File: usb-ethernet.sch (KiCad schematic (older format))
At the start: 17 parts

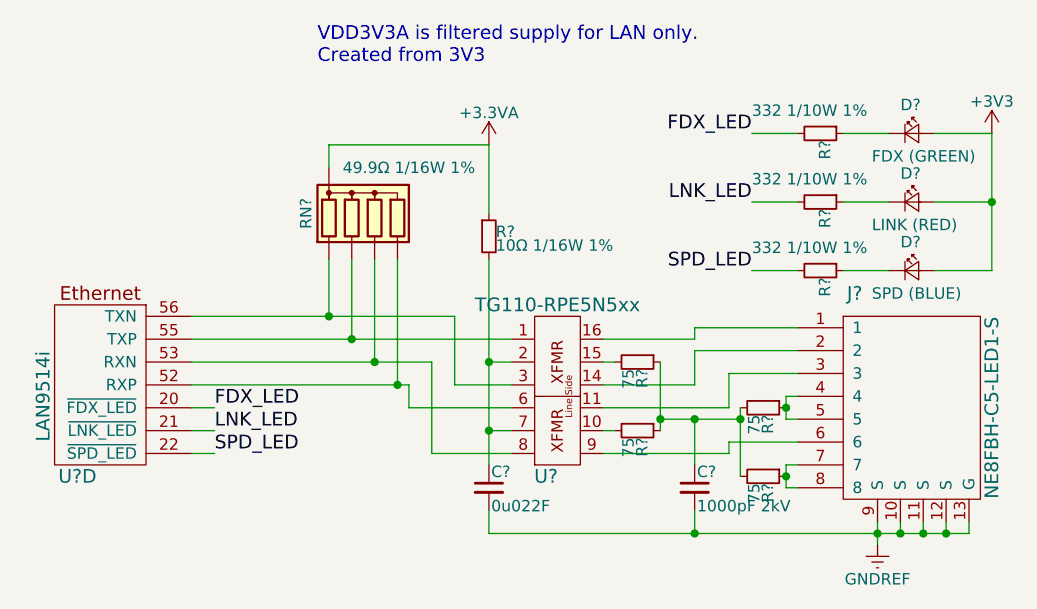
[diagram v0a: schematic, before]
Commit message: Started fixing DRC issues
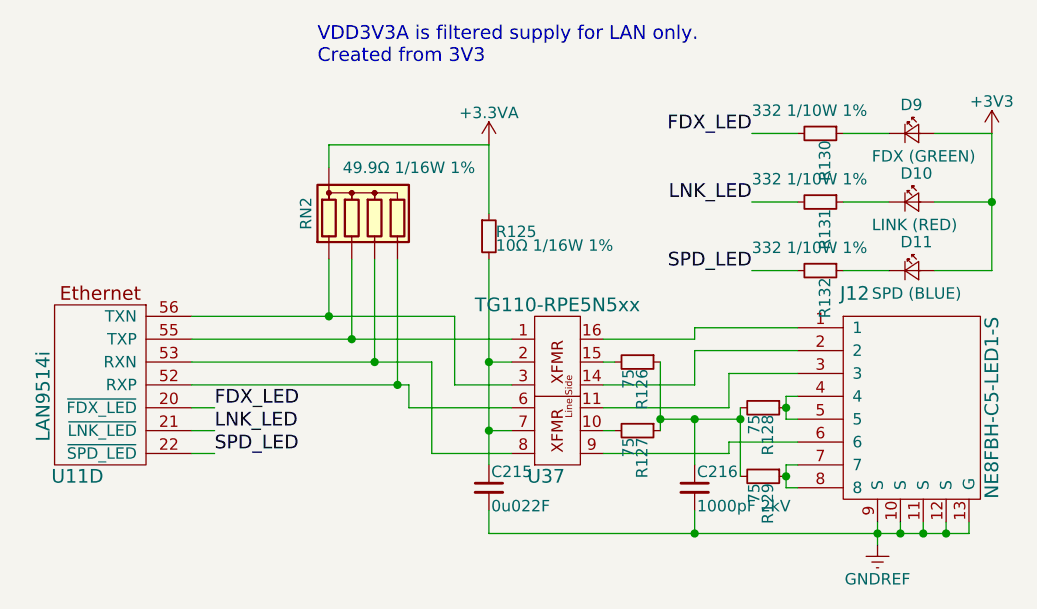
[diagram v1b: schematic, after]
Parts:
- C215, C216: renamed from C?; footprint (none) -> Capacitors_SMD:C_0603_HandSoldering
- R125, R126, R127, R128, R129, R130, R131, R132: renamed from R?; footprint (none) -> Capacitors_SMD:C_0603_HandSoldering
- U11: renamed from U?; footprint (none) -> Housings_DFN_QFN:QFN-64-1EP_9x9mm_Pitch0.5mm
- gave numbers to parts that had none: 6
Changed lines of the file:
@@
 P 3550 3750
 AR Path="/58DEDA35/5903ABC9" Ref="U?"  Part="4"
-AR Path="/58DEDA35/5903AB75/5903ABC9" Ref="U?"  Part="4"
-F 0 "U?" H 3650 3350 60  0000 C CNN
+AR Path="/58DEDA35/5903AB75/5903ABC9" Ref="U11"  Part="4"
+F 0 "U11" H 3650 3350 60  0000 C CNN
 F 1 "LAN9514i" V 3800 3700 60  0000 C CNN
-F 2 "" H 4250 4250 60  0001 C CNN
+F 2 "Housings_DFN_QFN:QFN-64-1EP_9x9mm_Pitch0.5mm" H 4250 4250 60  0001 C CNN
 F 3 "http://ww1.microchip.com/downloads/en/DeviceDoc/00002306A.pdf" H 3700 5400 60  0001 C CNN
 F 4 "Microchip Technology" H 3450 5100 60  0001 C CNN "Manufacturer"
@@
 $EndComp
 $Comp
-L TG110-RPE5N5xx U?
+L TG110-RPE5N5xx U37
 U 1 1 590032EB
 P 5550 3800
-F 0 "U?" H 5500 4150 60  0000 C CNN
+F 0 "U37" H 5500 4150 60  0000 C CNN
 F 1 "TG110-RPE5N5xx" H 5550 3400 60  0000 C CNN
 F 2 "" H 5050 4000 60  0001 C CNN
@@
 $EndComp
 $Comp
-L NE8FBH-C5-LED1-S J?
+L NE8FBH-C5-LED1-S J12
 U 1 1 5900332E
 P 7100 3800
-F 0 "J?" H 6850 4250 60  0000 C CNN
+F 0 "J12" H 6850 4250 60  0000 C CNN
 F 1 "NE8FBH-C5-LED1-S" V 7450 3750 60  0000 C CNN
 F 2 "" H 7000 3700 60  0001 C CNN
@@
 $EndComp
 $Comp
-L R_Small R?
+L R_Small R126
 U 1 1 5900376D
 P 5900 3650
-F 0 "R?" H 5930 3670 50  0000 L CNN
+F 0 "R126" H 5930 3670 50  0000 L CNN
 F 1 "75" H 5930 3610 50  0000 L CNN
-F 2 "" H 5900 3650 50  0001 C CNN
+F 2 "Capacitors_SMD:C_0603_HandSoldering" H 5900 3650 50  0001 C CNN
 F 3 "" H 5900 3650 50  0001 C CNN
 	1    5900 3650
@@
 $EndComp
 $Comp
-L R_Small R?
+L R_Small R127
 U 1 1 590037C5
 P 5900 3950
-F 0 "R?" H 5930 3970 50  0000 L CNN
+F 0 "R127" H 5930 3970 50  0000 L CNN
 F 1 "75" H 5930 3910 50  0000 L CNN
-F 2 "" H 5900 3950 50  0001 C CNN
+F 2 "Capacitors_SMD:C_0603_HandSoldering" H 5900 3950 50  0001 C CNN
 F 3 "" H 5900 3950 50  0001 C CNN
 	1    5900 3950
@@
 $EndComp
 $Comp
-L R_Small R?
+L R_Small R128
 U 1 1 5900382C
 P 6450 3850
-F 0 "R?" H 6480 3870 50  0000 L CNN
+F 0 "R128" H 6480 3870 50  0000 L CNN
 F 1 "75" H 6480 3810 50  0000 L CNN
-F 2 "" H 6450 3850 50  0001 C CNN
+F 2 "Capacitors_SMD:C_0603_HandSoldering" H 6450 3850 50  0001 C CNN
 F 3 "" H 6450 3850 50  0001 C CNN
 	1    6450 3850
@@
 $EndComp
 $Comp
-L R_Small R?
+L R_Small R129
 U 1 1 59003855
 P 6450 4150
-F 0 "R?" H 6480 4170 50  0000 L CNN
+F 0 "R129" H 6480 4170 50  0000 L CNN
 F 1 "75" H 6480 4110 50  0000 L CNN
-F 2 "" H 6450 4150 50  0001 C CNN
+F 2 "Capacitors_SMD:C_0603_HandSoldering" H 6450 4150 50  0001 C CNN
 F 3 "" H 6450 4150 50  0001 C CNN
 	1    6450 4150
@@
 $EndComp
 $Comp
-L C_Small C?
+L C_Small C216
 U 1 1 5900394D
 P 6150 4200
-F 0 "C?" H 6160 4270 50  0000 L CNN
+F 0 "C216" H 6160 4270 50  0000 L CNN
 F 1 "1000pF 2kV" H 6160 4120 50  0000 L CNN
-F 2 "" H 6150 4200 50  0001 C CNN
+F 2 "Capacitors_SMD:C_0603_HandSoldering" H 6150 4200 50  0001 C CNN
 F 3 "" H 6150 4200 50  0001 C CNN
 F 4 "0.00@0" H 6150 4200 60  0001 C CNN "Pricing"
@@
 $EndComp
 $Comp
-L GNDREF #PWR?
+L GNDREF #PWR0163
 U 1 1 59003AB4
 P 6950 4450
-F 0 "#PWR?" H 6950 4200 50  0001 C CNN
+F 0 "#PWR0163" H 6950 4200 50  0001 C CNN
 F 1 "GNDREF" H 6950 4300 50  0000 C CNN
 F 2 "" H 6950 4450 50  0001 C CNN
@@
 $EndComp
 $Comp
-L R_Small R?
+L R_Small R125
 U 1 1 59003EAC
 P 5250 3100
-F 0 "R?" H 5280 3120 50  0000 L CNN
+F 0 "R125" H 5280 3120 50  0000 L CNN
 F 1 "10Ω 1/16W 1%" H 5280 3060 50  0000 L CNN
-F 2 "" H 5250 3100 50  0001 C CNN
+F 2 "Capacitors_SMD:C_0603_HandSoldering" H 5250 3100 50  0001 C CNN
 F 3 "" H 5250 3100 50  0001 C CNN
 F 4 "0.00@0" H 5250 3100 60  0001 C CNN "Pricing"
@@
 $EndComp
 $Comp
-L R_Network04 RN?
+L R_Network04 RN2
 U 1 1 5900455A
 P 4750 3000
-F 0 "RN?" V 4450 3000 50  0000 C CNN
+F 0 "RN2" V 4450 3000 50  0000 C CNN
 F 1 "49.9Ω 1/16W 1%" H 4900 3200 50  0000 C CNN
 F 2 "Resistors_THT:R_Array_SIP5" V 5025 3000 50  0001 C CNN
@@
 $EndComp
 $Comp
-L LED_Small D?
+L LED_Small D10
 U 1 1 59005A5F
 P 7100 2950
-F 0 "D?" H 7050 3075 50  0000 L CNN
+F 0 "D10" H 7050 3075 50  0000 L CNN
 F 1 "LINK (RED)" H 6925 2850 50  0000 L CNN
 F 2 "" V 7100 2950 50  0001 C CNN
@@
 $EndComp
 $Comp
-L LED_Small D?
+L LED_Small D11
 U 1 1 59005AF2
 P 7100 3250
-F 0 "D?" H 7050 3375 50  0000 L CNN
+F 0 "D11" H 7050 3375 50  0000 L CNN
 F 1 "SPD (BLUE)" H 6925 3150 50  0000 L CNN
 F 2 "" V 7100 3250 50  0001 C CNN
@@
 $EndComp
 $Comp
-L LED_Small D?
+L LED_Small D9
 U 1 1 59005B83
 P 7100 2650
-F 0 "D?" H 7050 2775 50  0000 L CNN
+F 0 "D9" H 7050 2775 50  0000 L CNN
 F 1 "FDX (GREEN)" H 6925 2550 50  0000 L CNN
 F 2 "" V 7100 2650 50  0001 C CNN
@@
 $EndComp
 $Comp
-L R_Small R?
+L R_Small R130
 U 1 1 59005DEC
 P 6700 2650
-F 0 "R?" H 6730 2670 50  0000 L CNN
+F 0 "R130" H 6730 2670 50  0000 L CNN
 F 1 "332 1/10W 1%" V 6600 2350 50  0000 L CNN
-F 2 "" H 6700 2650 50  0001 C CNN
+F 2 "Capacitors_SMD:C_0603_HandSoldering" H 6700 2650 50  0001 C CNN
 F 3 "" H 6700 2650 50  0001 C CNN
 	1    6700 2650
@@
 $EndComp
 $Comp
-L R_Small R?
+L R_Small R131
 U 1 1 59005EDB
 P 6700 2950
-F 0 "R?" H 6730 2970 50  0000 L CNN
+F 0 "R131" H 6730 2970 50  0000 L CNN
 F 1 "332 1/10W 1%" V 6600 2650 50  0000 L CNN
-F 2 "" H 6700 2950 50  0001 C CNN
+F 2 "Capacitors_SMD:C_0603_HandSoldering" H 6700 2950 50  0001 C CNN
 F 3 "" H 6700 2950 50  0001 C CNN
 	1    6700 2950
@@
 $EndComp
 $Comp
-L R_Small R?
+L R_Small R132
 U 1 1 59005F1A
 P 6700 3250
-F 0 "R?" H 6730 3270 50  0000 L CNN
+F 0 "R132" H 6730 3270 50  0000 L CNN
 F 1 "332 1/10W 1%" V 6600 2950 50  0000 L CNN
-F 2 "" H 6700 3250 50  0001 C CNN
+F 2 "Capacitors_SMD:C_0603_HandSoldering" H 6700 3250 50  0001 C CNN
 F 3 "" H 6700 3250 50  0001 C CNN
 	1    6700 3250
@@
 $EndComp
 $Comp
-L +3V3 #PWR?
+L +3V3 #PWR0164
 U 1 1 590063C0
 P 7450 2650
-F 0 "#PWR?" H 7450 2500 50  0001 C CNN
+F 0 "#PWR0164" H 7450 2500 50  0001 C CNN
 F 1 "+3V3" H 7450 2790 50  0000 C CNN
 F 2 "" H 7450 2650 50  0001 C CNN
@@
 	6400 2950 6600 2950
 $Comp
-L C_Small C?
+L C_Small C215
 U 1 1 5901000F
 P 5250 4200
-F 0 "C?" H 5260 4270 50  0000 L CNN
+F 0 "C215" H 5260 4270 50  0000 L CNN
 F 1 "0u022F" H 5260 4120 50  0000 L CNN
-F 2 "" H 5250 4200 50  0001 C CNN
+F 2 "Capacitors_SMD:C_0603_HandSoldering" H 5250 4200 50  0001 C CNN
 F 3 "" H 5250 4200 50  0001 C CNN
 F 4 "0.00@0" H 5250 4200 60  0001 C CNN "Pricing"
@@
 Connection ~ 6150 4400
 $Comp
-L +3.3VA #PWR?
+L +3.3VA #PWR0165
 U 1 1 590123B2
 P 5250 2700
-F 0 "#PWR?" H 5250 2550 50  0001 C CNN
+F 0 "#PWR0165" H 5250 2550 50  0001 C CNN
 F 1 "+3.3VA" H 5250 2840 50  0000 C CNN
 F 2 "" H 5250 2700 50  0001 C CNN

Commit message: Finished first pass on power distro, annotated USB C controllers
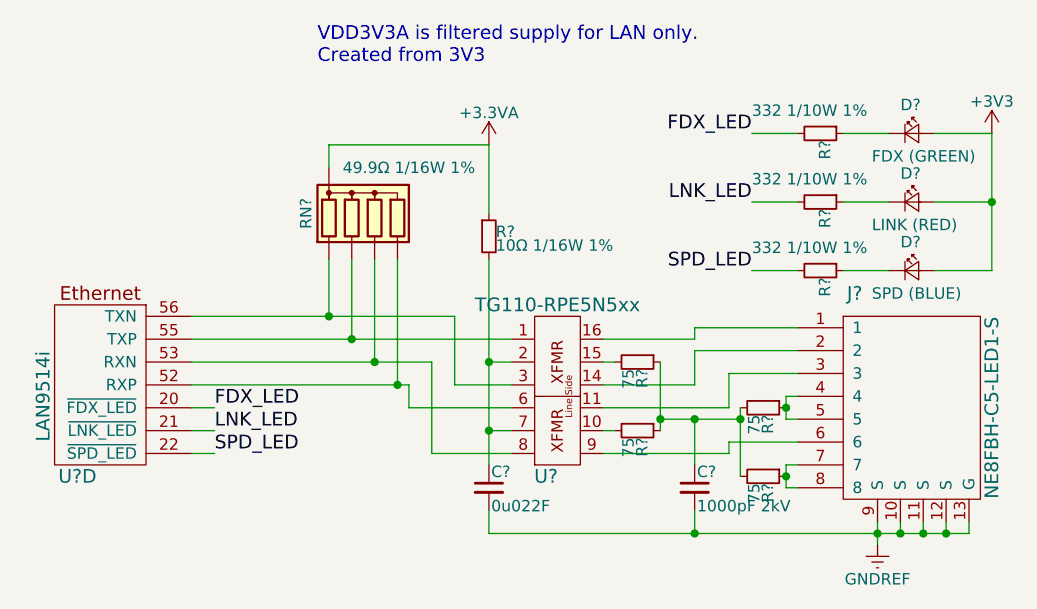
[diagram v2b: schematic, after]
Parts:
- renumbered C216 to C?, C215 to C?, D10 to D?, D11 to D?, D9 to D?, J12 to J?, R126 to R?, R127 to R?, R128 to R?, R129 to R?, R125 to R?, R130 to R?, R131 to R?, R132 to R?, RN2 to RN?, U37 to U?, U11 to U?
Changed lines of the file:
@@
 P 3550 3750
 AR Path="/58DEDA35/5903ABC9" Ref="U?"  Part="4"
-AR Path="/58DEDA35/5903AB75/5903ABC9" Ref="U11"  Part="4"
-F 0 "U11" H 3650 3350 60  0000 C CNN
+AR Path="/58DEDA35/5903AB75/5903ABC9" Ref="U?"  Part="4"
+F 0 "U?" H 3650 3350 60  0000 C CNN
 F 1 "LAN9514i" V 3800 3700 60  0000 C CNN
 F 2 "Housings_DFN_QFN:QFN-64-1EP_9x9mm_Pitch0.5mm" H 4250 4250 60  0001 C CNN
@@
 $EndComp
 $Comp
-L TG110-RPE5N5xx U37
+L TG110-RPE5N5xx U?
 U 1 1 590032EB
 P 5550 3800
-F 0 "U37" H 5500 4150 60  0000 C CNN
+F 0 "U?" H 5500 4150 60  0000 C CNN
 F 1 "TG110-RPE5N5xx" H 5550 3400 60  0000 C CNN
 F 2 "" H 5050 4000 60  0001 C CNN
@@
 $EndComp
 $Comp
-L NE8FBH-C5-LED1-S J12
+L NE8FBH-C5-LED1-S J?
 U 1 1 5900332E
 P 7100 3800
-F 0 "J12" H 6850 4250 60  0000 C CNN
+F 0 "J?" H 6850 4250 60  0000 C CNN
 F 1 "NE8FBH-C5-LED1-S" V 7450 3750 60  0000 C CNN
 F 2 "" H 7000 3700 60  0001 C CNN
@@
 $EndComp
 $Comp
-L R_Small R126
+L R_Small R?
 U 1 1 5900376D
 P 5900 3650
-F 0 "R126" H 5930 3670 50  0000 L CNN
+F 0 "R?" H 5930 3670 50  0000 L CNN
 F 1 "75" H 5930 3610 50  0000 L CNN
 F 2 "Capacitors_SMD:C_0603_HandSoldering" H 5900 3650 50  0001 C CNN
@@
 $EndComp
 $Comp
-L R_Small R127
+L R_Small R?
 U 1 1 590037C5
 P 5900 3950
-F 0 "R127" H 5930 3970 50  0000 L CNN
+F 0 "R?" H 5930 3970 50  0000 L CNN
 F 1 "75" H 5930 3910 50  0000 L CNN
 F 2 "Capacitors_SMD:C_0603_HandSoldering" H 5900 3950 50  0001 C CNN
@@
 $EndComp
 $Comp
-L R_Small R128
+L R_Small R?
 U 1 1 5900382C
 P 6450 3850
-F 0 "R128" H 6480 3870 50  0000 L CNN
+F 0 "R?" H 6480 3870 50  0000 L CNN
 F 1 "75" H 6480 3810 50  0000 L CNN
 F 2 "Capacitors_SMD:C_0603_HandSoldering" H 6450 3850 50  0001 C CNN
@@
 $EndComp
 $Comp
-L R_Small R129
+L R_Small R?
 U 1 1 59003855
 P 6450 4150
-F 0 "R129" H 6480 4170 50  0000 L CNN
+F 0 "R?" H 6480 4170 50  0000 L CNN
 F 1 "75" H 6480 4110 50  0000 L CNN
 F 2 "Capacitors_SMD:C_0603_HandSoldering" H 6450 4150 50  0001 C CNN
@@
 $EndComp
 $Comp
-L C_Small C216
+L C_Small C?
 U 1 1 5900394D
 P 6150 4200
-F 0 "C216" H 6160 4270 50  0000 L CNN
+F 0 "C?" H 6160 4270 50  0000 L CNN
 F 1 "1000pF 2kV" H 6160 4120 50  0000 L CNN
 F 2 "Capacitors_SMD:C_0603_HandSoldering" H 6150 4200 50  0001 C CNN
@@
 $EndComp
 $Comp
-L GNDREF #PWR0163
+L GNDREF #PWR?
 U 1 1 59003AB4
 P 6950 4450
-F 0 "#PWR0163" H 6950 4200 50  0001 C CNN
+F 0 "#PWR?" H 6950 4200 50  0001 C CNN
 F 1 "GNDREF" H 6950 4300 50  0000 C CNN
 F 2 "" H 6950 4450 50  0001 C CNN
@@
 $EndComp
 $Comp
-L R_Small R125
+L R_Small R?
 U 1 1 59003EAC
 P 5250 3100
-F 0 "R125" H 5280 3120 50  0000 L CNN
+F 0 "R?" H 5280 3120 50  0000 L CNN
 F 1 "10Ω 1/16W 1%" H 5280 3060 50  0000 L CNN
 F 2 "Capacitors_SMD:C_0603_HandSoldering" H 5250 3100 50  0001 C CNN
@@
 $EndComp
 $Comp
-L R_Network04 RN2
+L R_Network04 RN?
 U 1 1 5900455A
 P 4750 3000
-F 0 "RN2" V 4450 3000 50  0000 C CNN
+F 0 "RN?" V 4450 3000 50  0000 C CNN
 F 1 "49.9Ω 1/16W 1%" H 4900 3200 50  0000 C CNN
 F 2 "Resistors_THT:R_Array_SIP5" V 5025 3000 50  0001 C CNN
@@
 $EndComp
 $Comp
-L LED_Small D10
+L LED_Small D?
 U 1 1 59005A5F
 P 7100 2950
-F 0 "D10" H 7050 3075 50  0000 L CNN
+F 0 "D?" H 7050 3075 50  0000 L CNN
 F 1 "LINK (RED)" H 6925 2850 50  0000 L CNN
 F 2 "" V 7100 2950 50  0001 C CNN
@@
 $EndComp
 $Comp
-L LED_Small D11
+L LED_Small D?
 U 1 1 59005AF2
 P 7100 3250
-F 0 "D11" H 7050 3375 50  0000 L CNN
+F 0 "D?" H 7050 3375 50  0000 L CNN
 F 1 "SPD (BLUE)" H 6925 3150 50  0000 L CNN
 F 2 "" V 7100 3250 50  0001 C CNN
@@
 $EndComp
 $Comp
-L LED_Small D9
+L LED_Small D?
 U 1 1 59005B83
 P 7100 2650
-F 0 "D9" H 7050 2775 50  0000 L CNN
+F 0 "D?" H 7050 2775 50  0000 L CNN
 F 1 "FDX (GREEN)" H 6925 2550 50  0000 L CNN
 F 2 "" V 7100 2650 50  0001 C CNN
@@
 $EndComp
 $Comp
-L R_Small R130
+L R_Small R?
 U 1 1 59005DEC
 P 6700 2650
-F 0 "R130" H 6730 2670 50  0000 L CNN
+F 0 "R?" H 6730 2670 50  0000 L CNN
 F 1 "332 1/10W 1%" V 6600 2350 50  0000 L CNN
 F 2 "Capacitors_SMD:C_0603_HandSoldering" H 6700 2650 50  0001 C CNN
@@
 $EndComp
 $Comp
-L R_Small R131
+L R_Small R?
 U 1 1 59005EDB
 P 6700 2950
-F 0 "R131" H 6730 2970 50  0000 L CNN
+F 0 "R?" H 6730 2970 50  0000 L CNN
 F 1 "332 1/10W 1%" V 6600 2650 50  0000 L CNN
 F 2 "Capacitors_SMD:C_0603_HandSoldering" H 6700 2950 50  0001 C CNN
@@
 $EndComp
 $Comp
-L R_Small R132
+L R_Small R?
 U 1 1 59005F1A
 P 6700 3250
-F 0 "R132" H 6730 3270 50  0000 L CNN
+F 0 "R?" H 6730 3270 50  0000 L CNN
 F 1 "332 1/10W 1%" V 6600 2950 50  0000 L CNN
 F 2 "Capacitors_SMD:C_0603_HandSoldering" H 6700 3250 50  0001 C CNN
@@
 $EndComp
 $Comp
-L +3V3 #PWR0164
+L +3V3 #PWR?
 U 1 1 590063C0
 P 7450 2650
-F 0 "#PWR0164" H 7450 2500 50  0001 C CNN
+F 0 "#PWR?" H 7450 2500 50  0001 C CNN
 F 1 "+3V3" H 7450 2790 50  0000 C CNN
 F 2 "" H 7450 2650 50  0001 C CNN
@@
 	6400 2950 6600 2950
 $Comp
-L C_Small C215
+L C_Small C?
 U 1 1 5901000F
 P 5250 4200
-F 0 "C215" H 5260 4270 50  0000 L CNN
+F 0 "C?" H 5260 4270 50  0000 L CNN
 F 1 "0u022F" H 5260 4120 50  0000 L CNN
 F 2 "Capacitors_SMD:C_0603_HandSoldering" H 5250 4200 50  0001 C CNN
@@
 Connection ~ 6150 4400
 $Comp
-L +3.3VA #PWR0165
+L +3.3VA #PWR?
 U 1 1 590123B2
 P 5250 2700
-F 0 "#PWR0165" H 5250 2550 50  0001 C CNN
+F 0 "#PWR?" H 5250 2550 50  0001 C CNN
 F 1 "+3.3VA" H 5250 2840 50  0000 C CNN
 F 2 "" H 5250 2700 50  0001 C CNN
